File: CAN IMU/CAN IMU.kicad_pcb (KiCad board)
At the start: 4 copper layers, 49.5 x 48.9 mm, 29 parts, among them J1 GPIO, J2 ADC, J3 CAN, J4 USB_A, SW1 SW_Push, SW2 SW_SPDT, U1 TJA1051T, U2 AMS1117-3.3, U3 STM32F103C4Tx, x1 8Mhz

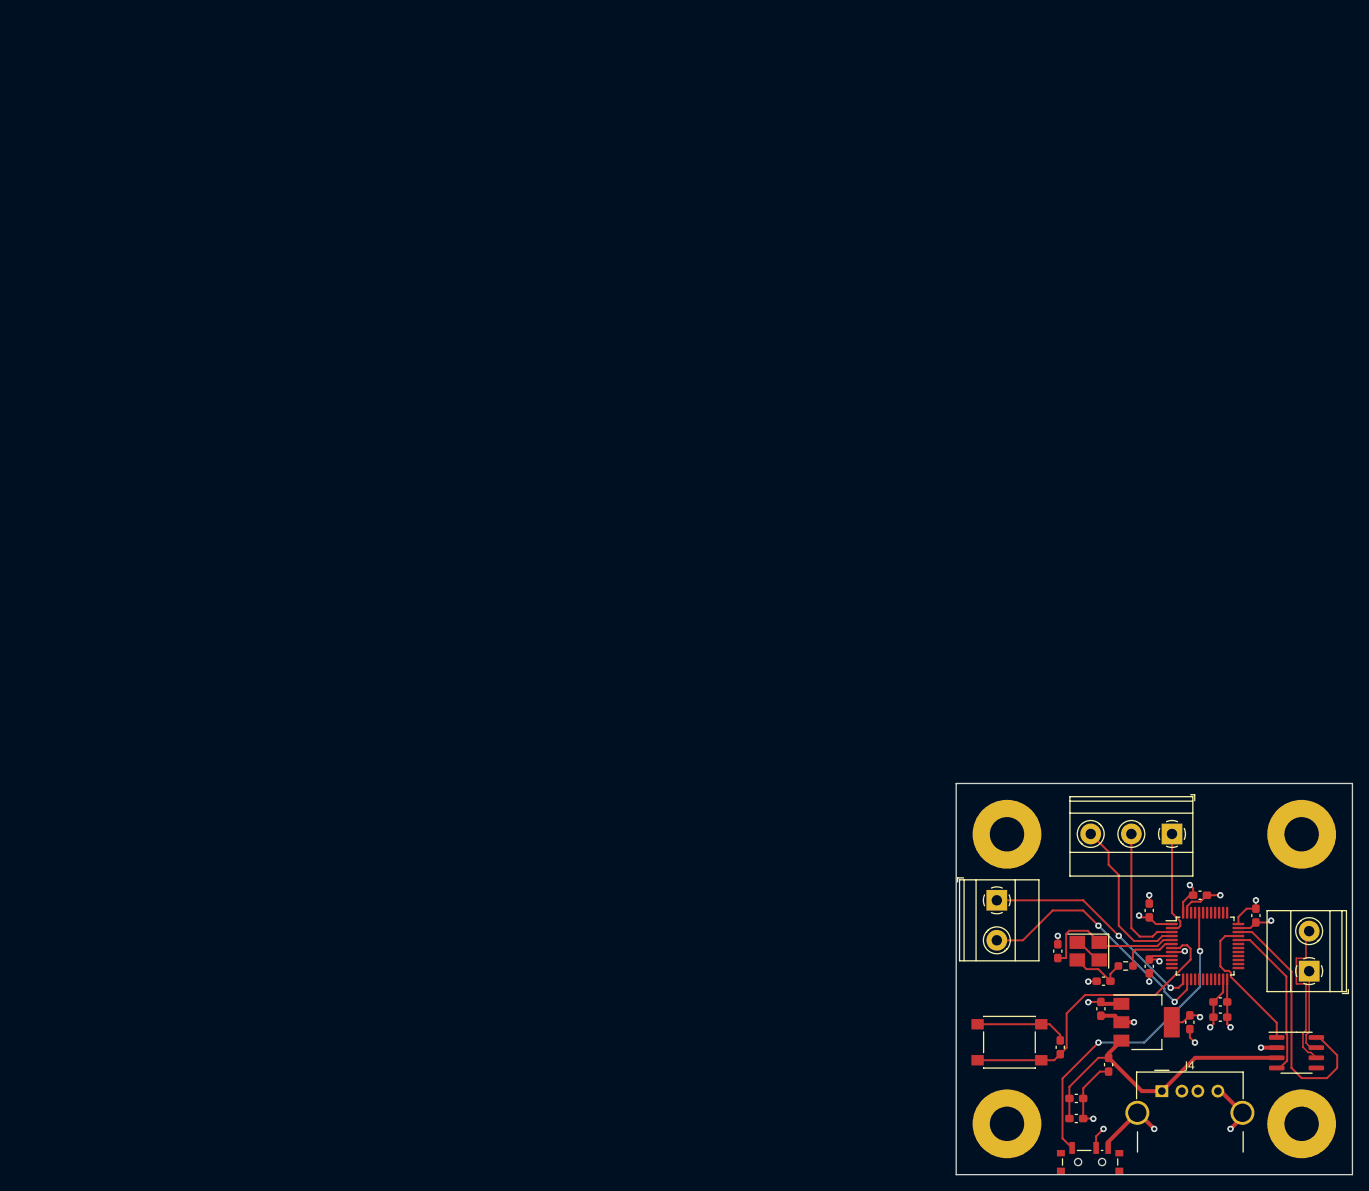
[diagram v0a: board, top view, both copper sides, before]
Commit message: redid the traces for the LSM6DSOX CAN PCB. Also created the BOM and the CPL files for manufacturing. Which means this board should be ready to get sent to pcb manufacturing.
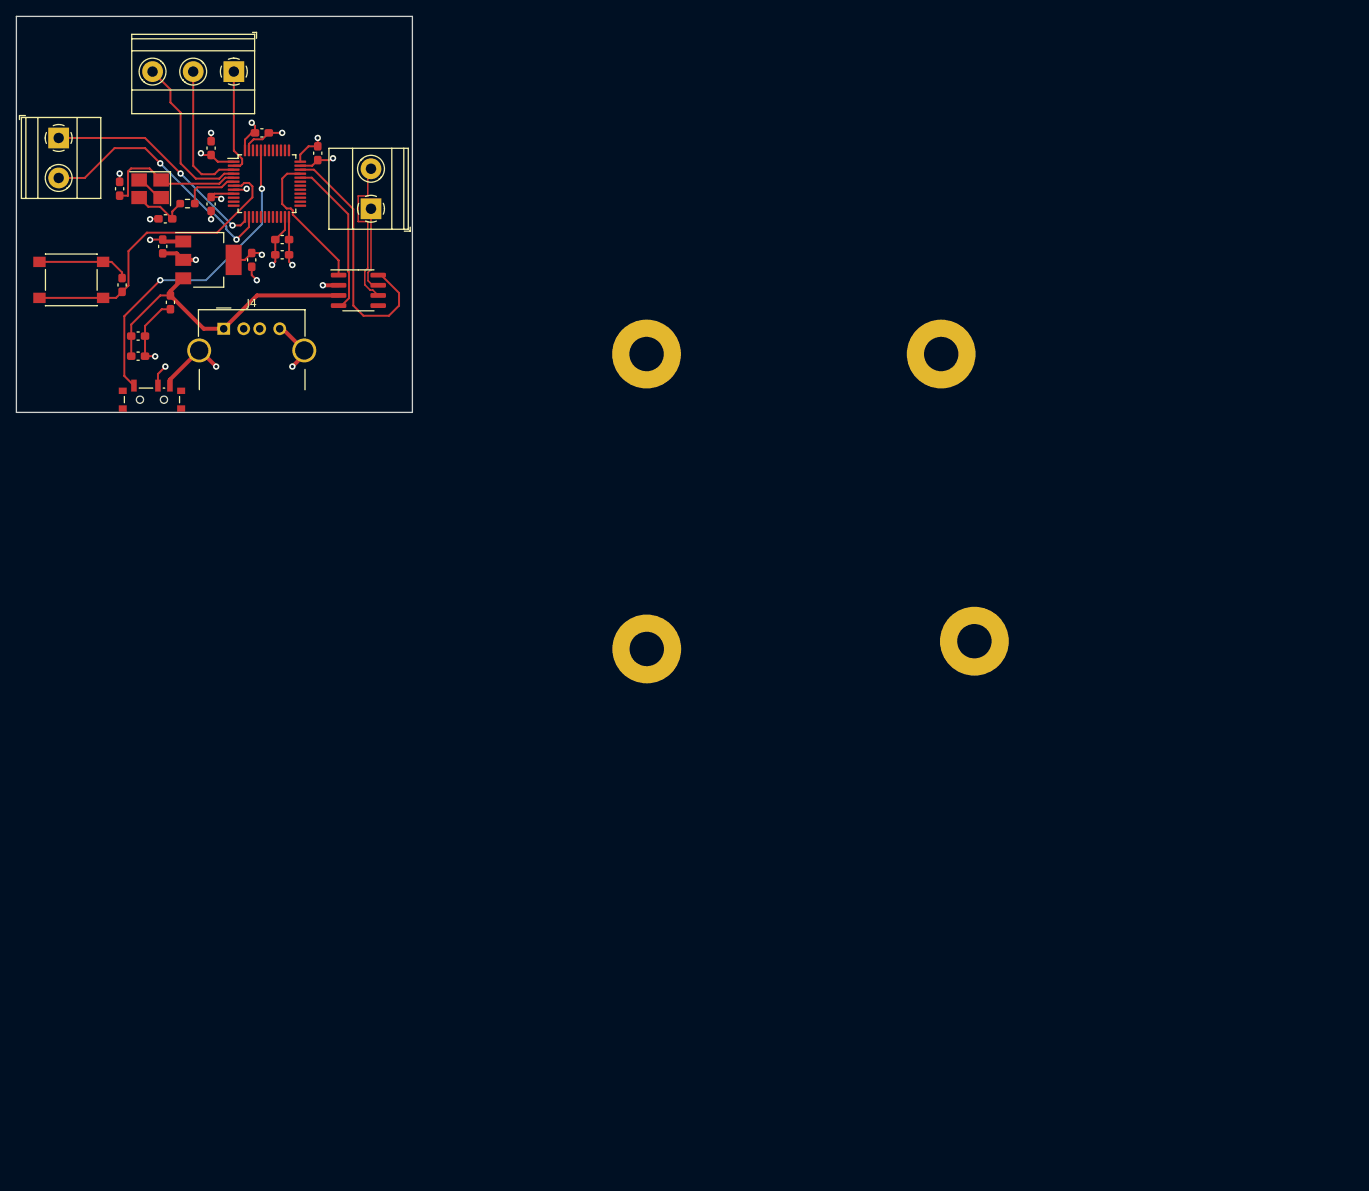
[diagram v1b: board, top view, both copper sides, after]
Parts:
- moved C10 151.1 mm to (33.2, 29.8)
- moved C12 151.1 mm to (29.4, 30.4)
- moved C4 151.1 mm to (12.9, 21.5)
- moved C7 151.1 mm to (30.7, 14.6)
- moved C9 151.1 mm to (33.2, 27.9)
- moved J4 151.1 mm to (25.9, 39.0)
- moved SW2 151.1 mm to (16.9, 47.6)
- moved U2 151.1 mm to (24.0, 30.4)
- moved U3 151.1 mm to (31.3, 20.9)
- moved x1 151.1 mm to (16.7, 21.5)
- moved C1 151.1 mm to (19.3, 35.7)
- moved C11 151.1 mm to (18.3, 28.8)
- moved C13 151.1 mm to (15.2, 40.0)
- moved C14 151.1 mm to (15.2, 42.5)
- moved C2 151.1 mm to (37.7, 17.1)
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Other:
- board size 49.5 x 48.9 mm -> 49.5 x 49.5 mm
